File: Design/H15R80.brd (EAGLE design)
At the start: 34.6 x 30 mm, 24 parts, among them P1 HEXABIT_17.32_NO_P3_P6, U1 STM32F091CBU6, U2 DAC8760IRHAR, X1 XTALL_CSTCE8M00G52

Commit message: Finished schematics
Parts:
- added C12, C15: 10.0uF, rcl:CT7343
- added C13, C16, C18, C19, C20, C22, C25, C31, C33: 100nF, Hexabitz:C-0603
- added C14, C17, C21, C23, C24, C32, C34: 100pF, Hexabitz:C-0603
- added C26, C27, C28, C29: DNP, Hexabitz:C-0603
- added C30: 22nF, Hexabitz:C-0603
- added R5: 10.0K, Hexabitz:R-0603
- added R6: 15.0K, Hexabitz:R-0603
- added U3: OPA192, Hexabitz:DBV0005A_N
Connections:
- removed net AVDD: U2.36
- removed net AVSS: U2.37
- removed net AVSS_2: U2.14
- removed net DVDD: U2.39
- removed net GND_2: U2.3
- removed net GND_3: U2.12
- removed net GND_4: U2.13
- removed net PAD: U2.41
- removed net UART1_RX: U1.P$31
- removed net UART1_TX: U1.P$30
- removed net UART2_RX: U1.P$13
- removed net UART2_TX: U1.P$12
- new net +15V: C12.+, C13.1, C14.1, C20.1, C21.1, C26.2, C27.2, C31.1, C32.1, PWR.3, U2.36, U3.5
- new net -15V: C15.-, C16.1, C17.1, C22.1, C23.1, C24.1, C25.1, C33.1, C34.1, PWR.1, U2.14, U2.37, U2.41, U3.2
- new net AGND: AO.2, C12.-, C13.2, C14.2, C15.+, C16.2, C17.2, C18.2, C19.2, C20.2, C21.2, C22.2, C23.2, C24.2, C25.2, C29.1, C30.2, C31.2, C32.2, C33.2, C34.2, PWR.2, R6.1, U2.12, U2.13, U2.15, U2.23, U2.3, U2.34, U2.4, U2.5
- new net AO_ALARM: R5.1, U1.P$29, U2.2
- new net N$1: AO.1, C28.2, C29.2, U2.26, U2.32, U3.3
- new net N$10: C27.1, U2.28
- new net N$11: C28.1, U2.24
- new net N$12: R6.2, U2.16
- new net N$13: U2.33, U3.1, U3.4
- new net N$14: C30.1, U2.25
- new net N$2: C19.1, U2.17, U2.18
- new net N$8: C26.1, U2.29
- new net SPI2_CS: U1.P$25, U2.6
- new net SPI2_MISO: U1.P$27, U2.9
- new net SPI2_MOSI: U1.P$28, U2.8
- new net SPI2_SCK: U1.P$26, U2.7
- new net UART1_RX*: P1.PAD_PD5, U1.P$31
- new net UART1_TX*: P1.PAD_PU5, U1.P$30
- new net UART2_RX*: P1.PAD_PD2, U1.P$13
- new net UART2_TX*: P1.PAD_PU2, U1.P$12
- net GND: no longer U2.15
- net UART3_RX: now also P1.PAD_PD4
- net UART3_TX: now also P1.PAD_PU4
- net UART5_RX: now also P1.PAD_PD1
- net UART5_TX: now also P1.PAD_PU1
- net VDD: now also C18.1, R5.2, U2.39

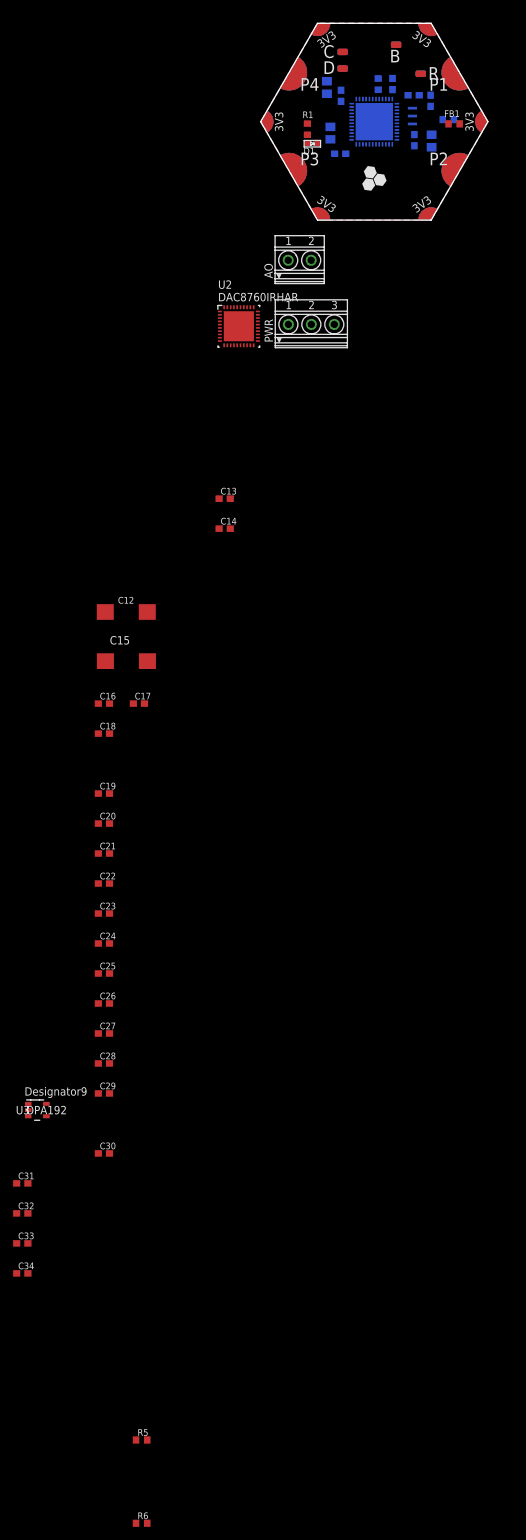
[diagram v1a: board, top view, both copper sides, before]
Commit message: Placed most components Routed analog routes
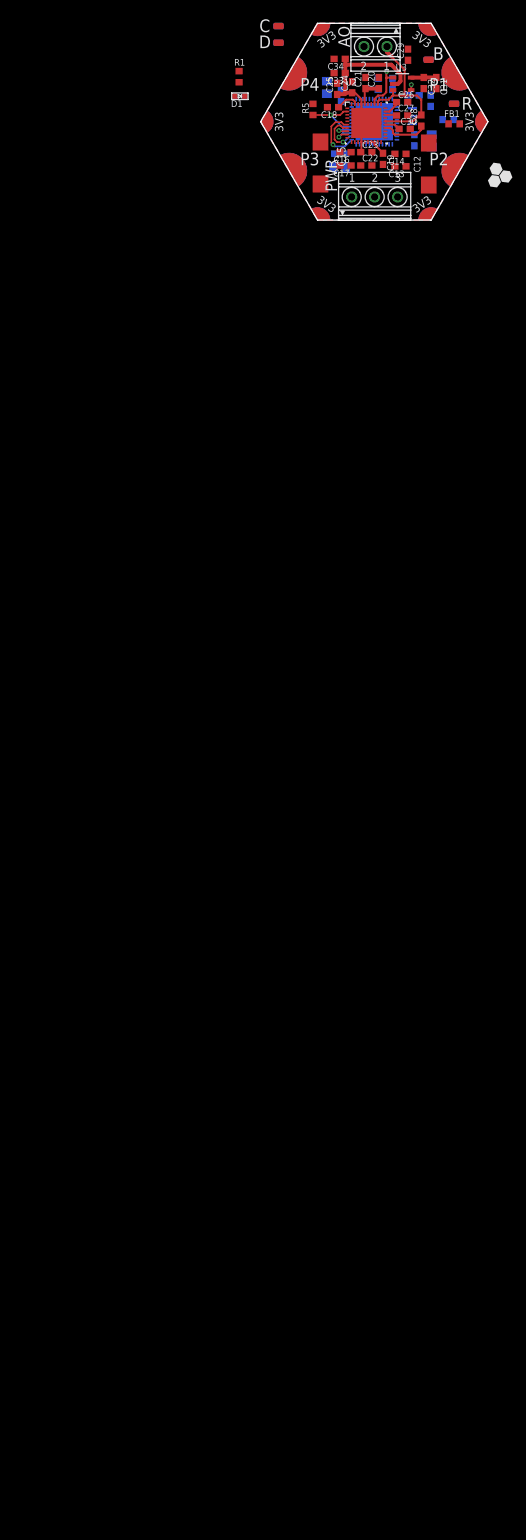
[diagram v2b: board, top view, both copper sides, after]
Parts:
- removed R6: 15.0K, Hexabitz:R-0603
- moved R5 204.5 mm to (25.3, 36.5), turned to 90 degrees
- moved C34 191.4 mm to (29.3, 44.2), turned to 180 degrees
- moved C33 184.9 mm to (29.3, 42.0), turned to 180 degrees
- moved C32 182.9 mm to (42.2, 40.5), turned to 270 degrees
- moved C31 179.2 mm to (44.1, 40.5), turned to 270 degrees
- moved U3 166.1 mm to (38.9, 40.4)
- moved C29 165.0 mm to (39.8, 44.8), turned to 90 degrees
- moved C30 162.8 mm to (39.2, 33.5)
- moved C28 151.7 mm to (41.8, 34.8), turned to 90 degrees
- moved C27 147.2 mm to (38.9, 35.6)
- moved C26 144.7 mm to (38.9, 37.6)
- moved C25 139.5 mm to (29.0, 39.6), turned to 90 degrees
- moved C24 135.9 mm to (31.2, 39.9), turned to 90 degrees
- moved C21 124.1 mm to (33.3, 40.5), turned to 90 degrees
- moved C23 122.8 mm to (33.4, 30.0)
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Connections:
- removed net N$12: R6.2, U2.16
- net AGND: no longer R6.1
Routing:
- net -15V: track 0.00 -> 29.4 mm
- net N$1: track 0.00 -> 25.5 mm
- net N$13: track 0.00 -> 14.2 mm, vias 0 -> 2
- net AO_ALARM: track 0.00 -> 9.41 mm, vias 0 -> 1
- net SPI2_CS: track 0.00 -> 9.15 mm, vias 0 -> 1
- net +15V: track 0.00 -> 8.27 mm
- net SPI2_SCK: track 0.00 -> 7.09 mm, vias 0 -> 1
- net N$11: track 0.00 -> 6.99 mm
- net SPI2_MISO: track 0.00 -> 3.67 mm, vias 0 -> 1
- net VDD: track 0.00 -> 3.43 mm
- net SPI2_MOSI: track 0.00 -> 3.34 mm, vias 0 -> 1
- net N$2: track 0.00 -> 2.75 mm
- net N$8: track 0.00 -> 2.50 mm
- net N$14: track 0.00 -> 2.36 mm
- net N$10: track 0.00 -> 1.76 mm
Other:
- board text added: "Total Thickness 1.6 mm --------------------------------------------------------- copper_top_l1.gbr : Top Conductor - Copper: Thickness 0.035 mm Dielectric - FR-4: Thickness 0.175 mm copper_inner_l2.gbr : GND Plane - Copper: Thickness 0.035 mm Dielectric - FR-4: Thickness 1.11 mm copper_inner_l3.gbr : VDD Plane - Copper: Thickness 0.035 mm Dielectric - FR-4: Thickness 0.175 mm copper_bottom_l4.gbr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"

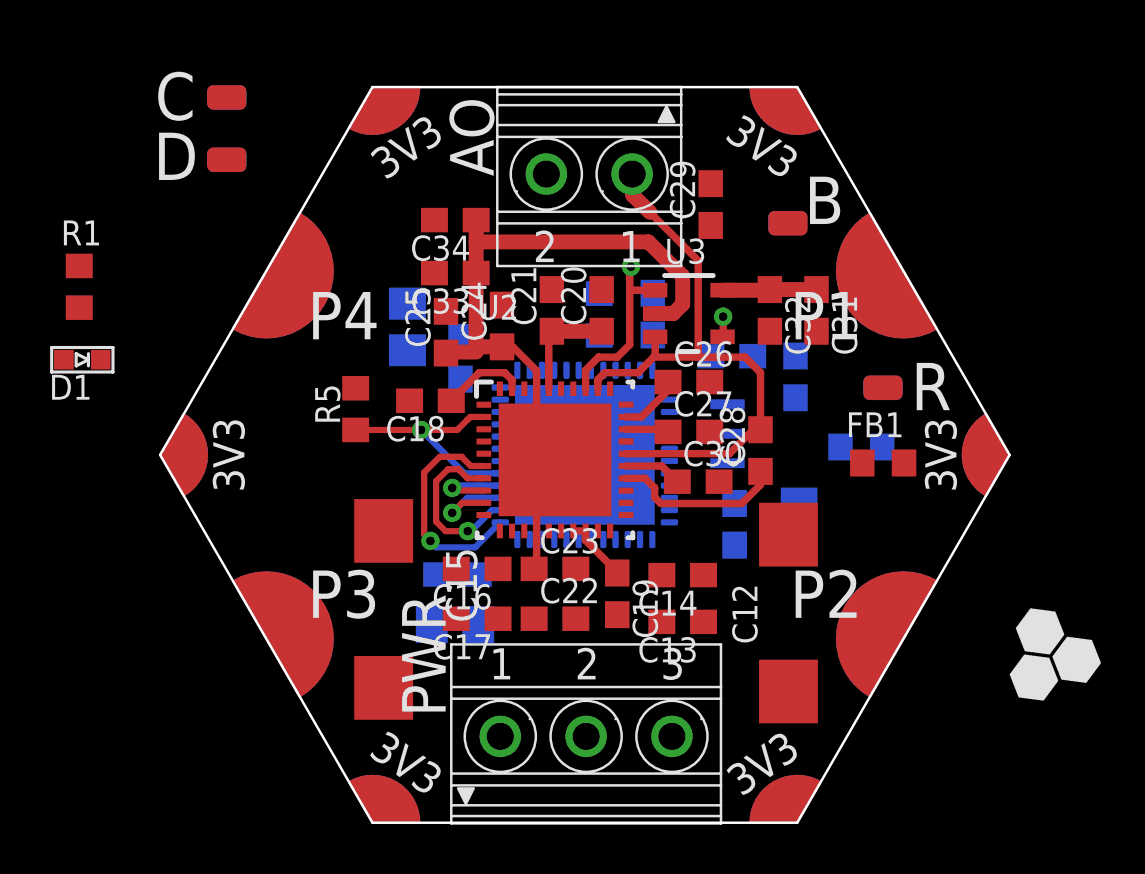
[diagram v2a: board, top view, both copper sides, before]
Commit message: Routing digital section
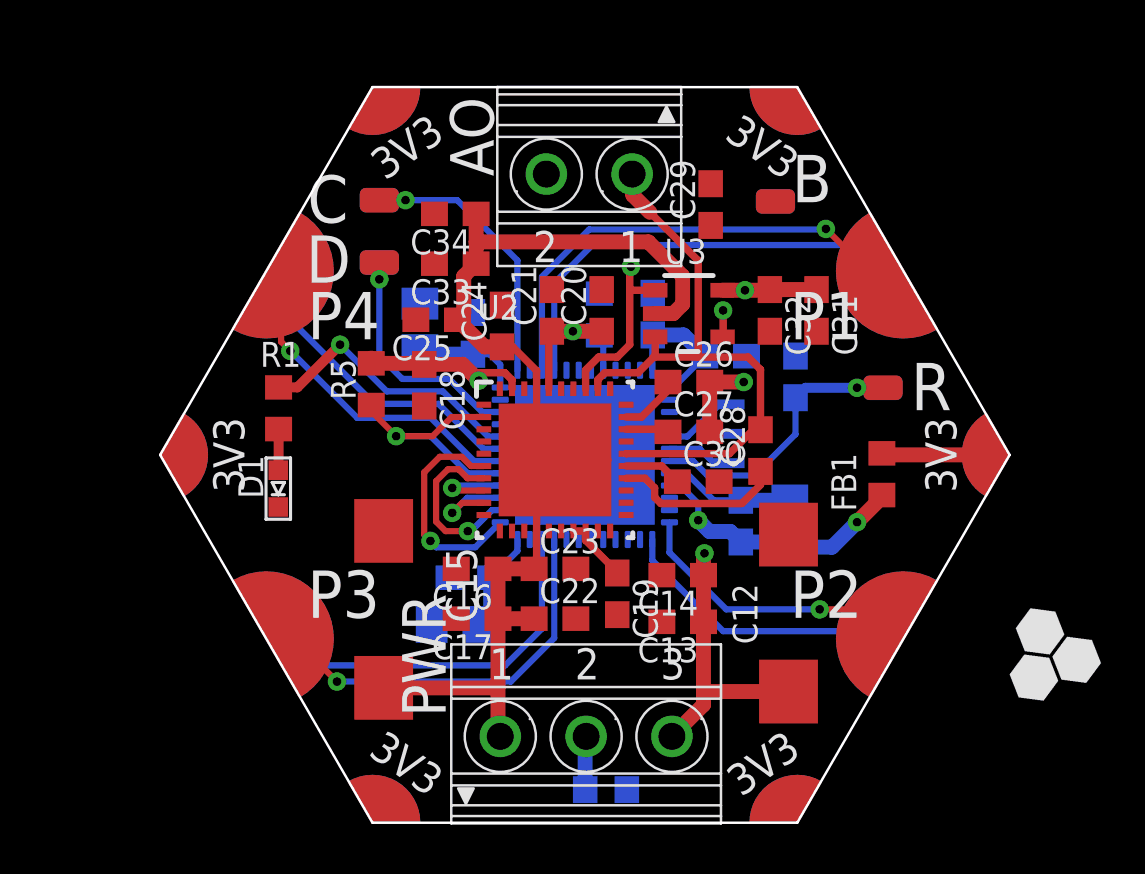
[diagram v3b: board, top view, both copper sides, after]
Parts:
- moved R2 17.4 mm to (35.5, 21.0)
- moved D1 9.56 mm to (22.1, 33.2), turned to 0 degrees
- moved R1 9.52 mm to (22.1, 36.5)
- moved C 7.50 mm to (26.2, 45.0)
- moved D 7.50 mm to (26.2, 42.5)
- moved R5 1.20 mm to (25.9, 37.5)
- moved C5 1.14 mm to (30.1, 39.6)
- moved B 1.02 mm to (42.4, 45.0)
- moved C18 0.68 mm to (28.1, 37.5), turned to 270 degrees
- moved C25 0.63 mm to (28.6, 40.1), turned to 180 degrees
- moved C6 0.52 mm to (29.9, 29.6)
- moved C7 0.51 mm to (27.9, 39.8)
- moved FB1 0.46 mm to (46.7, 33.8), turned to 90 degrees
- moved C2 0.40 mm to (43.0, 31.8)
- moved C33 0.38 mm to (29.3, 42.4)
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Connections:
- removed net AGND: AO.2, C12.-, C13.2, C14.2, C15.+, C16.2, C17.2, C18.2, C19.2, C20.2, C21.2, C22.2, C23.2, C24.2, C25.2, C29.1, C30.2, C31.2, C32.2, C33.2, C34.2, PWR.2, U2.12, U2.13, U2.15, U2.23, U2.3, U2.34, U2.4, U2.5
- net VDD: no longer C18.1, R5.2, U2.39
- net VDDA: now also C18.1, R5.2, U2.39
- net VSSA: now also AO.2, C12.-, C13.2, C14.2, C15.+, C16.2, C17.2, C18.2, C19.2, C20.2, C21.2, C22.2, C23.2, C24.2, C25.2, C29.1, C30.2, C31.2, C32.2, C33.2, C34.2, PWR.2, U2.12, U2.13, U2.15, U2.23, U2.3, U2.34, U2.4, U2.5
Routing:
- net +15V: track 8.27 -> 41.6 mm, vias 0 -> 4
- net VDDA: track 0.00 -> 30.8 mm, vias 0 -> 3
- net UART5_TX: track 0.00 -> 19.6 mm, vias 0 -> 1
- net UART5_RX: track 0.00 -> 18.4 mm
- net UART3_TX: track 0.00 -> 16.8 mm, vias 0 -> 1
- net UART3_RX: track 0.00 -> 15.5 mm
- net VDD: track 3.43 -> 18.9 mm
- net -15V: track 29.4 -> 43.4 mm
- net UART1_TX*: track 0.00 -> 13.5 mm, vias 0 -> 1
- net UART1_RX*: track 0.00 -> 12.5 mm
- net R1: track 0.00 -> 12.4 mm, vias 0 -> 1
- net N$9: track 0.00 -> 12.2 mm, vias 0 -> 1
- net UART2_RX*: track 0.00 -> 11.7 mm
- net UART2_TX*: track 0.00 -> 11.5 mm, vias 0 -> 1
- net N$3: track 0.00 -> 11.3 mm, vias 0 -> 1
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
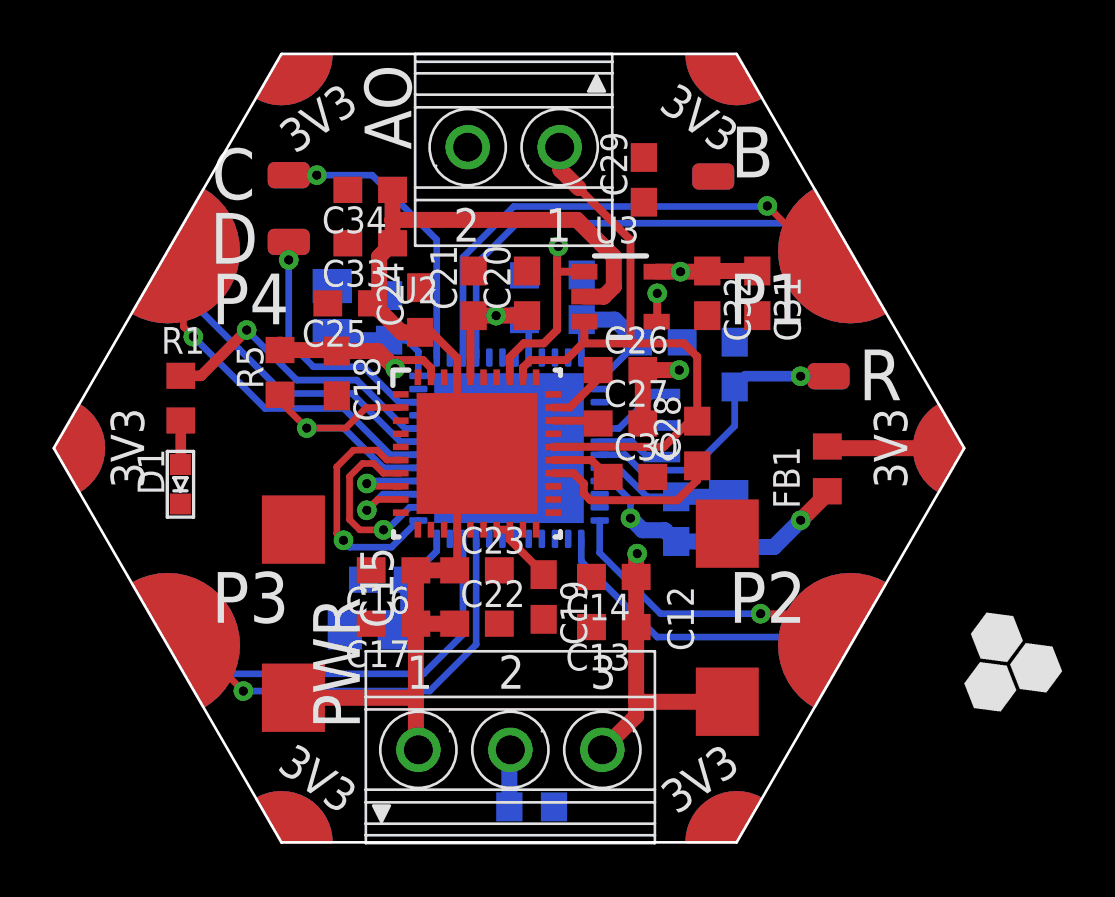
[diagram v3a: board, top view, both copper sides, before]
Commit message: Finished routing and silkscreen placement
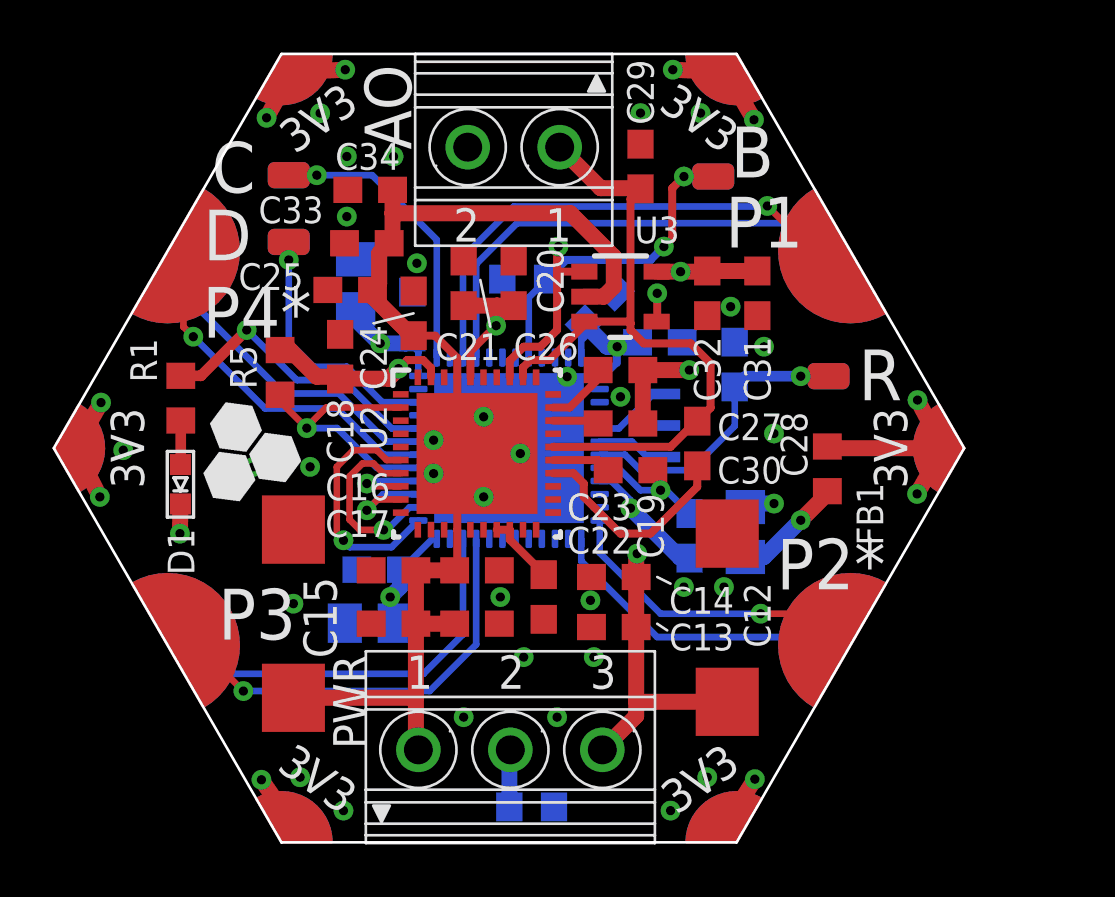
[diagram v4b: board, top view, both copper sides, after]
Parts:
- U2: value DAC8760IRHAR -> DAC8760RHA
- moved C7 1.35 mm to (28.8, 40.9)
- moved C5 0.90 mm to (30.9, 39.7)
- moved C1 0.81 mm to (41.5, 31.3)
- moved C3 0.80 mm to (38.1, 40.0), turned to 135 degrees
- moved C2 0.74 mm to (43.6, 31.4)
- moved R3 0.70 mm to (35.2, 41.1), turned to 180 degrees
- moved C18 0.65 mm to (28.2, 38.1), turned to 90 degrees
- moved C20 0.63 mm to (34.8, 40.9)
- moved C21 0.54 mm to (32.9, 40.9)
- moved C29 0.52 mm to (39.6, 45.3), turned to 270 degrees
- moved C25 0.51 mm to (28.6, 40.6)
- moved C6 0.46 mm to (29.7, 30.0)
- moved C24 0.28 mm to (31.0, 39.8)
- moved C30 0.25 mm to (39.2, 33.8)
- moved C4 0.25 mm to (29.3, 28.0)
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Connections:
- net GND: now also U1.P$16, U1.P$17, U1.P$18, U1.P$19, U1.P$2, U1.P$20, U1.P$3, U1.P$38, U1.P$4, U1.P$41, U1.P$42, U1.P$43
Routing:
- net VDD: track 18.9 -> 127.2 mm, vias 0 -> 13
- net B1: track 1.49 -> 13.4 mm, vias 0 -> 2
- net VSSA: track 7.55 -> 9.70 mm, vias 0 -> 17
- net -15V: track 43.4 -> 45.2 mm, vias 0 -> 5
- net +15V: track 41.6 -> 43.3 mm
- net VDDA: track 30.8 -> 29.5 mm
- net N$11: track 6.99 -> 8.27 mm
- net GND: track 0.00 -> 1.13 mm, vias 0 -> 19
- net N$1: track 25.6 -> 26.4 mm
- added copper zone on layer 2, net -15V
- added copper zone on layer 15, net GND
- added copper zone on layer 1, net VSSA
- added copper zone on layer 2, net VSSA
- removed copper zone on layer 1, net VDD
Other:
- board text added: "+15V"
- board text added: "-15V"
- board text added: "P2*"
- board text added: "P4*"
- board text added: "V/I+"
- board text added: "V/I-"
- board text removed: "P2"
- board text removed: "P4"

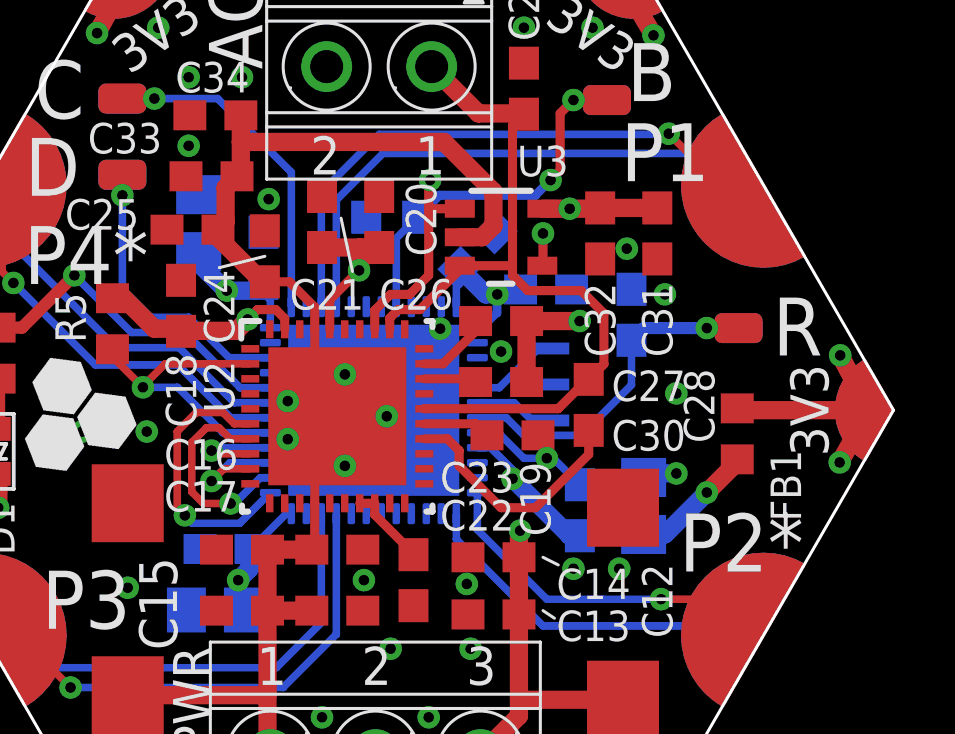
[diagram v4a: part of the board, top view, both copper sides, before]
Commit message: Solved DRC
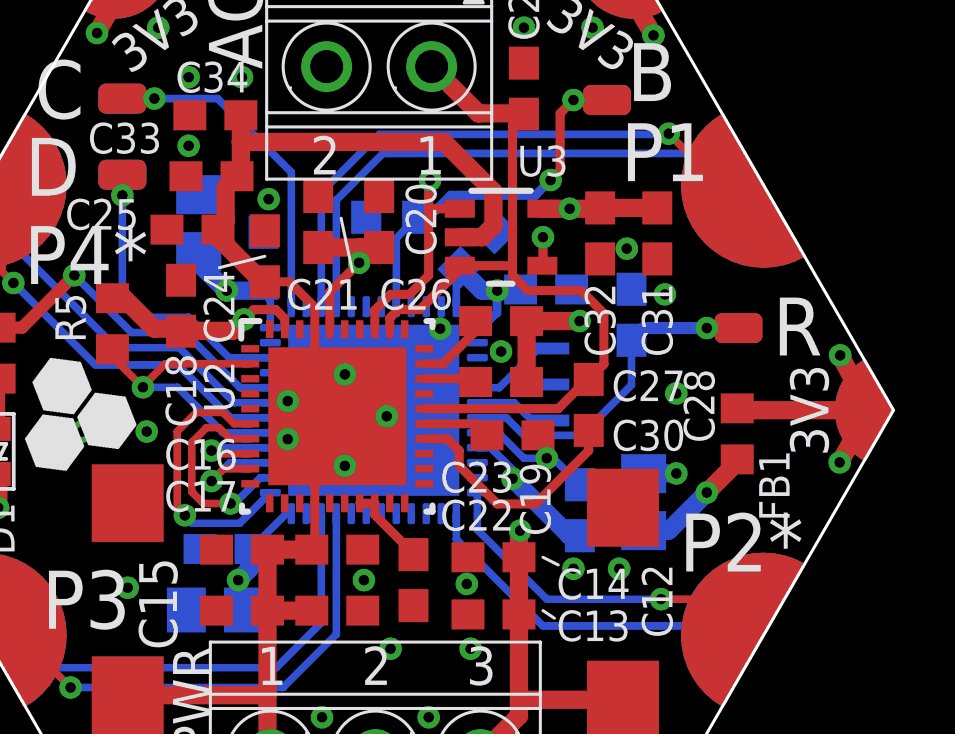
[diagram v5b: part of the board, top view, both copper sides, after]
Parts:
- moved C21 0.13 mm to (32.8, 40.9)
- moved C2 0.13 mm to (43.6, 31.6)
